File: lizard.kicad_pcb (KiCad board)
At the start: 2 copper layers, 14.8 x 56.2 mm, 11 parts, among them P1 SW DBG, U1 EFM8BB1

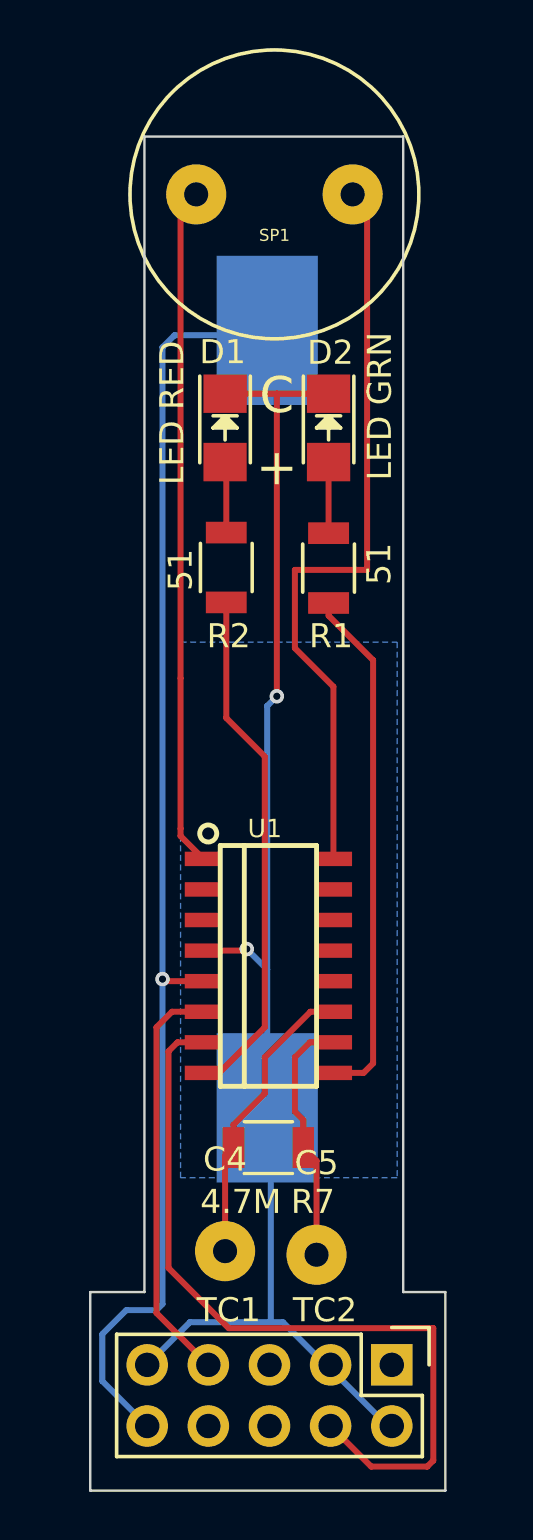
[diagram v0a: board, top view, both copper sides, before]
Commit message: did relayout for new battery holder; shrunk board dramatically; simplified layout
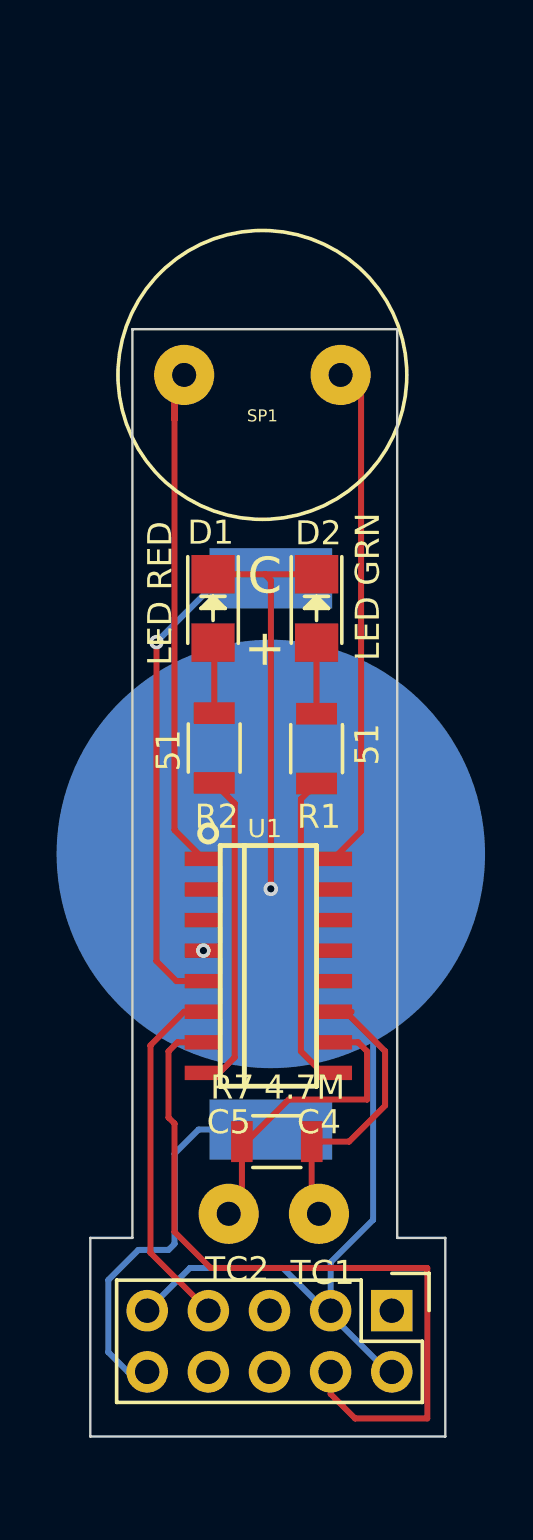
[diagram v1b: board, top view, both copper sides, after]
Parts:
- BT1: footprint mpd-bu2032-sm:MPD-BU2032-SM -> linx-bat-hld-001:linx-bat-hld-001
- moved D1 7.52 mm to (118.8, 111.3)
- moved D2 7.52 mm to (123.2, 111.3)
- moved R1 7.52 mm to (123.2, 117.2)
- moved R2 7.52 mm to (118.9, 117.2)
- moved SP1 7.52 mm to (120.9, 101.7)
- moved BT1 5.60 mm to (121.2, 121.5), turned to 90 degrees
- moved C4 4.20 mm to (123.2, 136.5)
- moved C5 4.03 mm to (119.5, 136.5)
- moved P1 2.25 mm to (126.3, 140.5)
- moved R7 0.43 mm to (121.5, 133.5), turned to 180 degrees
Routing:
- net VDD: track 53.7 -> 39.7 mm
- net Net-(SP1-Pad1): track 31.5 -> 21.8 mm
- net GND: track 59.3 -> 68.1 mm
- net Net-(R1-Pad2): track 21.7 -> 13.1 mm
- net Net-(R2-Pad2): track 21.6 -> 13.3 mm
- net Net-(SP1-Pad2): track 28.3 -> 22.2 mm
- net Net-(C5-Pad1): track 10.4 -> 13.1 mm
- net Net-(P1-Pad7): track 17.1 -> 14.8 mm
- net Net-(P1-Pad4): track 33.9 -> 32.6 mm
- removed copper zone on B.Cu, net GND
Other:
- board size 14.8 x 56.2 mm -> 14.8 x 46 mm
- board text added: "1.0c"
- board text added: "Desert Lizard v1.0c http://github.com"
- board text removed: "1.0b"
- board text removed: "Desert Lizard Board v1.0b Copyright © 2015 Bart Massey http://github.com/DesertLizard/LizardBoard"

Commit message: made minor tweaks to layout pre-cut
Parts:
- moved BT1 0.35 mm to (120.9, 121.5)
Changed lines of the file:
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@@
-(kicad_pcb (version 4) (host pcbnew "(2015-06-09 BZR 5726)-product")
+(kicad_pcb (version 4) (host pcbnew "(2015-08-06 BZR 6058)-product")
   (general
     (links 21)
     (no_connects 1)
-    (area 113.699999 99.699999 128.550001 148.050001)
+    (area 109.457857 95.374999 256.507142 200.3)
     (thickness 1.6)
     (drawings 16)
@@
   (module Wire_Pads:SolderWirePad_single_1mmDrill (layer F.Cu)
     (at 123.25 136.5)
-    (fp_text reference C4 (at 0 -3.81) (layer F.SilkS)
-      (effects (font (size 1 1) (thickness 0.15)))
-    )
-    (fp_text value TC1 (at 0.15 2.45) (layer F.SilkS)
+    (fp_text reference C4 (at 0 -3.81) (layer F.SilkS) hide
+      (effects (font (size 1 1) (thickness 0.15)))
+    )
+    (fp_text value TC1 (at 2.35 1.8) (layer F.SilkS)
       (effects (font (size 1 1) (thickness 0.15)))
     )
@@
   (module Wire_Pads:SolderWirePad_single_1mmDrill (layer F.Cu)
     (at 119.5 136.5)
-    (fp_text reference C5 (at 0 -3.81) (layer F.SilkS)
-      (effects (font (size 1 1) (thickness 0.15)))
-    )
-    (fp_text value TC2 (at 0.35 2.3) (layer F.SilkS)
+    (fp_text reference C5 (at 0 -3.81) (layer F.SilkS) hide
+      (effects (font (size 1 1) (thickness 0.15)))
+    )
+    (fp_text value TC2 (at -2.3 1.8) (layer F.SilkS)
       (effects (font (size 1 1) (thickness 0.15)))
     )
@@
     (tags "resistor 1206")
     (attr smd)
-    (fp_text reference R7 (at 1.85 2.25 180) (layer F.SilkS)
-      (effects (font (size 1 1) (thickness 0.15)))
-    )
-    (fp_text value 4.7M (at -1.15 2.25 180) (layer F.SilkS)
+    (fp_text reference R7 (at 3.75 0.5 270) (layer F.SilkS)
+      (effects (font (size 1 1) (thickness 0.15)))
+    )
+    (fp_text value 4.7M (at -3.5 0 270) (layer F.SilkS)
       (effects (font (size 1 1) (thickness 0.15)))
     )
@@
   )
   (module linx-bat-hld-001:linx-bat-hld-001 (layer B.Cu)
-    (at 121.25 121.55 90)
-    (fp_text reference BT1 (at 0 -10.16 90) (layer B.SilkS)
+    (at 120.9 121.5 90)
+    (fp_text reference BT1 (at 0 -10.16 90) (layer B.SilkS) hide
       (effects (font (size 1 1) (thickness 0.15)) (justify mirror))
     )
-    (fp_text value BATTERY (at 0 10.16 90) (layer B.Fab)
+    (fp_text value BATTERY (at 0 10.16 90) (layer B.SilkS) hide
       (effects (font (size 1 1) (thickness 0.15)) (justify mirror))
     )

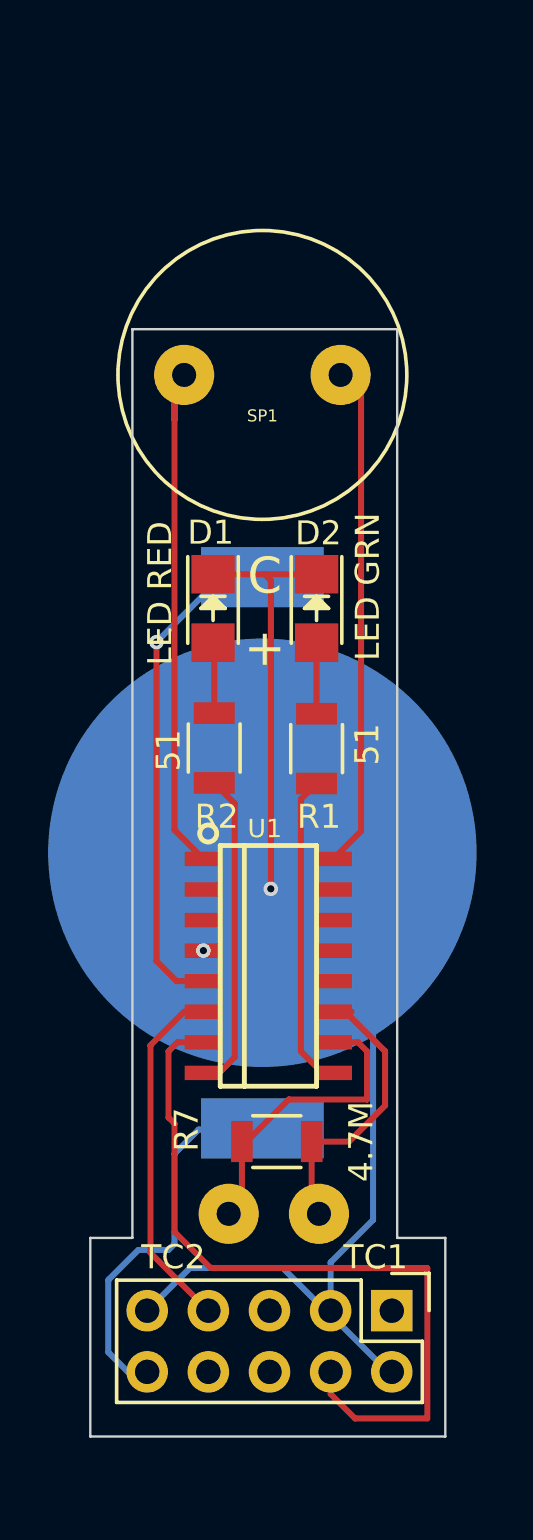
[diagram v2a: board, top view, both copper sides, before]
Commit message: prepped for OSH Park; need to fix battery ground
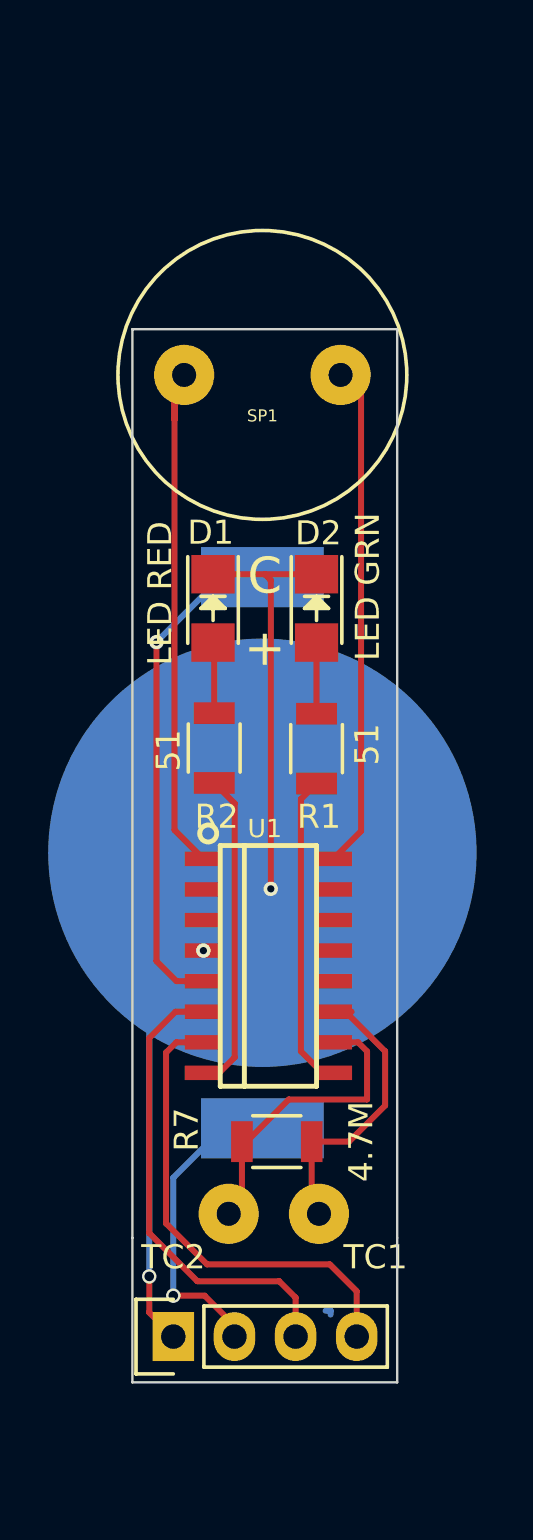
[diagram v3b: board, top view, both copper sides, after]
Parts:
- P1: value SW DBG -> DEBUG; footprint Pin_Headers:Pin_Header_Straight_2x05 -> Pin_Headers:Pin_Header_Straight_1x04
- moved P1 9.14 mm to (117.2, 141.6), turned to 90 degrees
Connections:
- P1 pad 1: Net-(P1-Pad1) -> GND
- P1 pad 2: GND -> VDD
- P1 pad 3: GND -> Net-(P1-Pad3)
- U1 pad 6: Net-(P1-Pad7) -> Net-(P1-Pad3)
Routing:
- net Net-(P1-Pad3): track 0.00 -> 19.6 mm
- net Net-(P1-Pad7): track 14.8 -> 0.00 mm
- net Net-(P1-Pad4): track 32.6 -> 19.8 mm
- net GND: track 68.1 -> 59.9 mm, vias 2 -> 3
- net VDD: track 39.7 -> 36.1 mm, vias 1 -> 2
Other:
- board size 14.8 x 46 mm -> 11 x 43.8 mm
- board text added: "Desert Lizard v1.1 http://github.com 2015-08-16"
- board text removed: "1.0c"
- board text removed: "2015-08-06"
- board text removed: "Desert Lizard board"
- board text removed: "Desert Lizard v1.0c http://github.com"
- board text removed: "lizard.kicad_pcb sheet 1/1"

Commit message: modified battery ground to fit board
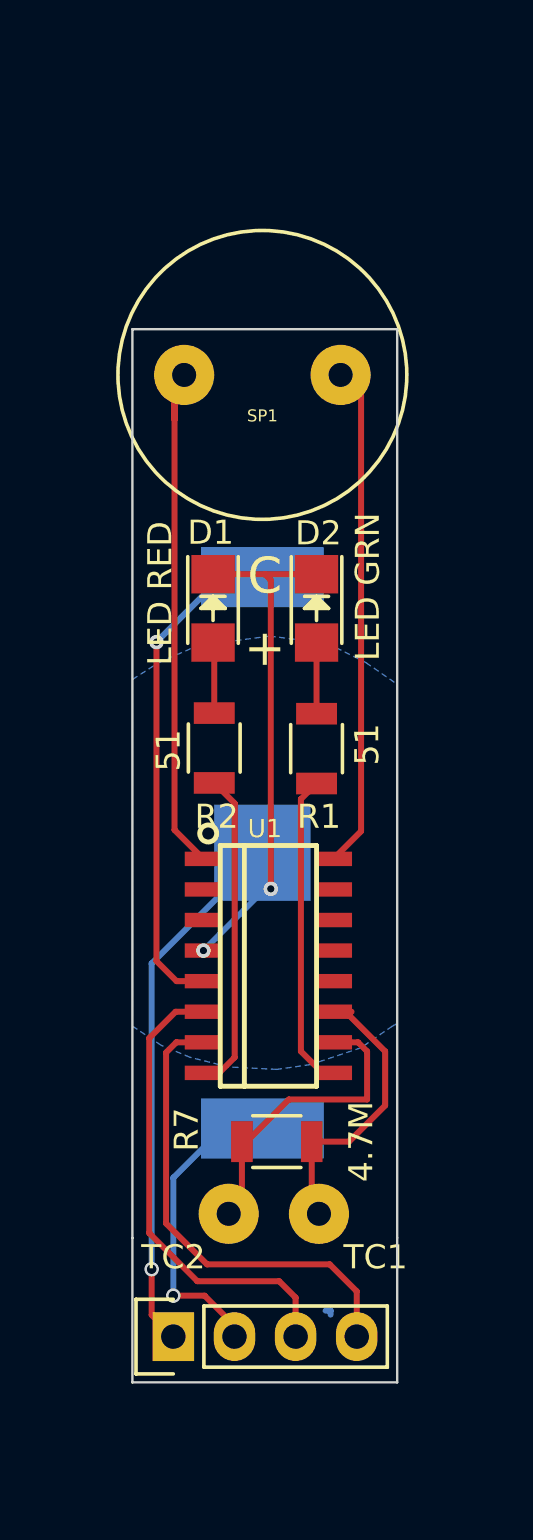
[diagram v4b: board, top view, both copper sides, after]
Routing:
- net GND: track 59.9 -> 43.8 mm
- added copper zone on B.Cu, net GND
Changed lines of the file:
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@@
     (thickness 1.6)
     (drawings 10)
-    (tracks 87)
+    (tracks 82)
     (zones 0)
     (modules 11)
@@
     (mod_text_size 1 1)
     (mod_text_width 0.15)
-    (pad_size 2.5 5.1)
+    (pad_size 4 4)
     (pad_drill 0)
     (pad_to_mask_clearance 0)
@@
       (effects (font (size 1 1) (thickness 0.15)) (justify mirror))
     )
-    (pad 2 smd circle (at 0 0 90) (size 17.8 17.8) (layers B.Cu B.Paste B.Mask)
+    (pad 2 smd rect (at 0 0 90) (size 4 4) (layers B.Cu B.Paste B.Mask)
       (net 2 GND))
     (pad 1 smd rect (at -11.45 0 90) (size 2.5 5.1) (layers B.Cu B.Paste B.Mask)
@@
   (segment (start 116.5 112.75) (end 119.15 110.1) (width 0.25) (layer B.Cu) (net 1))
   (segment (start 118.45 126.835) (end 117.335 126.835) (width 0.25) (layer F.Cu) (net 1))
-  (segment (start 117.2 141.6) (end 116.2 140.6) (width 0.25) (layer F.Cu) (net 2))
-  (segment (start 116.2 139.1) (end 116.2 126.2) (width 0.25) (layer B.Cu) (net 2))
-  (via (at 116.2 139.1) (size 0.6) (drill 0.4) (layers F.Cu B.Cu) (net 2))
-  (segment (start 116.2 140.6) (end 116.2 139.1) (width 0.25) (layer F.Cu) (net 2))
-  (segment (start 116.2 126.2) (end 120.9 121.5) (width 0.25) (layer B.Cu) (net 2))
-  (segment (start 121.25 121.55) (end 124.5 118.3) (width 0.25) (layer B.Cu) (net 2))
-  (segment (start 125.5 125.8) (end 121.25 121.55) (width 0.25) (layer B.Cu) (net 2))
-  (segment (start 121.25 124.25) (end 121.25 121.55) (width 0.25) (layer B.Cu) (net 2))
-  (segment (start 121.25 122.765) (end 121.25 121.55) (width 0.25) (layer B.Cu) (net 2))
+  (segment (start 117.2 141.6) (end 116.3 140.7) (width 0.25) (layer F.Cu) (net 2))
+  (segment (start 116.3 138.8) (end 116.3 126.1) (width 0.25) (layer B.Cu) (net 2))
+  (via (at 116.3 138.8) (size 0.6) (drill 0.4) (layers F.Cu B.Cu) (net 2))
+  (segment (start 116.3 140.7) (end 116.3 138.8) (width 0.25) (layer F.Cu) (net 2))
+  (segment (start 116.3 126.1) (end 120.9 121.5) (width 0.25) (layer B.Cu) (net 2))
   (segment (start 118.45 125.565) (end 121.25 122.765) (width 0.25) (layer B.Cu) (net 2))
   (via (at 118.45 125.565) (size 0.6) (layers F.Cu B.Cu) (net 2))
@@
   (segment (start 121.25 110.18014) (end 121.25 123) (width 0.25) (layer F.Cu) (net 2))
   (via (at 121.25 123) (size 0.6) (layers F.Cu B.Cu) (net 2))
-  (segment (start 121.25 123) (end 121.25 121.55) (width 0.25) (layer B.Cu) (net 2))
   (segment (start 121 109.93014) (end 121.25 110.18014) (width 0.25) (layer F.Cu) (net 2))
   (segment (start 123.85 128.105) (end 124.355 128.105) (width 0.25) (layer F.Cu) (net 3))
@@
   (segment (start 121.6 139.3) (end 118.2 139.3) (width 0.25) (layer F.Cu) (net 13))
   (segment (start 122.28 139.98) (end 121.6 139.3) (width 0.25) (layer F.Cu) (net 13))
+  (zone (net 2) (net_name GND) (layer B.Cu) (hatch edge 0.508)
+    (connect_pads yes (clearance 0.508))
+    (min_thickness 0.254)
+    (fill yes (arc_segments 16) (thermal_gap 0.508) (thermal_bridge_width 0.508))
+    (polygon
+      (pts
+        (xy 123.6 112.8) (xy 125.2 113.6) (xy 126.5 114.5) (xy 126.5 128.6) (xy 126.3 128.7)
+        (xy 125 129.6) (xy 122.9 130.3) (xy 121.5 130.5) (xy 119.5 130.4) (xy 117.9 130)
+        (xy 116.7 129.5) (xy 115.5 128.7) (xy 115.5 114.3) (xy 116.6 113.6) (xy 118.2 112.9)
+        (xy 121.2 112.5) (xy 123.6 112.8)
+      )
+    )
+  )
 )

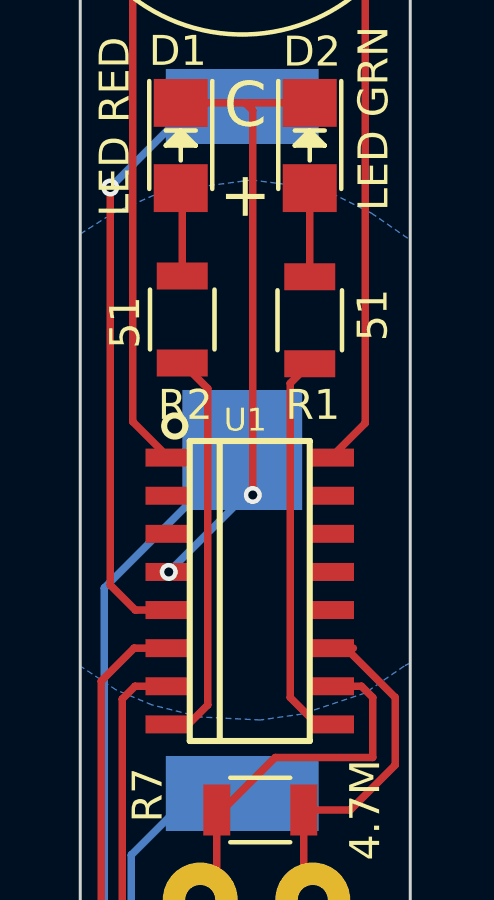
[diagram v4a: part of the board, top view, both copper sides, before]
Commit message: replaced battery ground fill covered by mask with big rectangular pad
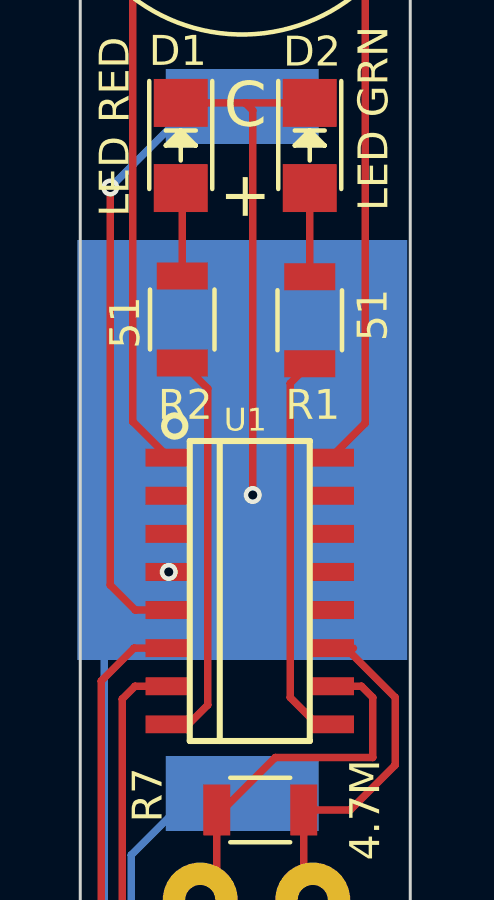
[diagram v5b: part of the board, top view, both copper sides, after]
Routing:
- removed copper zone on B.Cu, net GND
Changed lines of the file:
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@@
     (links 19)
     (no_connects 1)
-    (area 115.449999 99.699999 126.550001 143.550001)
+    (area 109.107857 95.374999 211.678576 181.3)
     (thickness 1.6)
     (drawings 10)
@@
     (mod_text_size 1 1)
     (mod_text_width 0.15)
-    (pad_size 4 4)
+    (pad_size 14 11)
     (pad_drill 0)
     (pad_to_mask_clearance 0)
@@
       (effects (font (size 1 1) (thickness 0.15)) (justify mirror))
     )
-    (pad 2 smd rect (at 0 0 90) (size 4 4) (layers B.Cu B.Paste B.Mask)
+    (pad 2 smd rect (at 0 0 90) (size 14 11) (layers B.Cu B.Paste B.Mask)
       (net 2 GND))
     (pad 1 smd rect (at -11.45 0 90) (size 2.5 5.1) (layers B.Cu B.Paste B.Mask)
@@
   (segment (start 121.6 139.3) (end 118.2 139.3) (width 0.25) (layer F.Cu) (net 13))
   (segment (start 122.28 139.98) (end 121.6 139.3) (width 0.25) (layer F.Cu) (net 13))
-  (zone (net 2) (net_name GND) (layer B.Cu) (hatch edge 0.508)
-    (connect_pads yes (clearance 0.508))
-    (min_thickness 0.254)
-    (fill yes (arc_segments 16) (thermal_gap 0.508) (thermal_bridge_width 0.508))
-    (polygon
-      (pts
-        (xy 123.6 112.8) (xy 125.2 113.6) (xy 126.5 114.5) (xy 126.5 128.6) (xy 126.3 128.7)
-        (xy 125 129.6) (xy 122.9 130.3) (xy 121.5 130.5) (xy 119.5 130.4) (xy 117.9 130)
-        (xy 116.7 129.5) (xy 115.5 128.7) (xy 115.5 114.3) (xy 116.6 113.6) (xy 118.2 112.9)
-        (xy 121.2 112.5) (xy 123.6 112.8)
-      )
-    )
-  )
 )
